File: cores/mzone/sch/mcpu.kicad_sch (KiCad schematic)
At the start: 45 parts

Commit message: mzone core
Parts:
- renumbered A_A13 to B_A13, A_A14 to B_A14, A_B12 to B_B12, A_B13 to B_B13, A_B7 to B_B7, A_C1 to B_C1, A_C10 to B_C10, A_C11 to B_C11, A_C12 to B_C12, A_C13 to B_C13, A_C9 to B_C9, A_D10 to B_D10, A_D14 to B_D14, A_D8 to B_D8, A_DE11 to B_DE11, A_DE12 to B_DE12, A_DE13 to B_DE13, A_DE9 to B_DE9, A_F10 to B_F10, A_F6 to B_F6, A_F9 to B_F9, A_FG14 to B_FG14, A_G6 to B_G6, A_G7 to B_G7, A_G8 to B_G8, A_G9 to B_G9, A_H10 to B_H10, A_H11 to B_H11, A_H12 to B_H12, A_H14 to B_H14, A_H6 to B_H6, A_H7 to B_H7, A_H8 to B_H8, A_RA7 to B_RA7

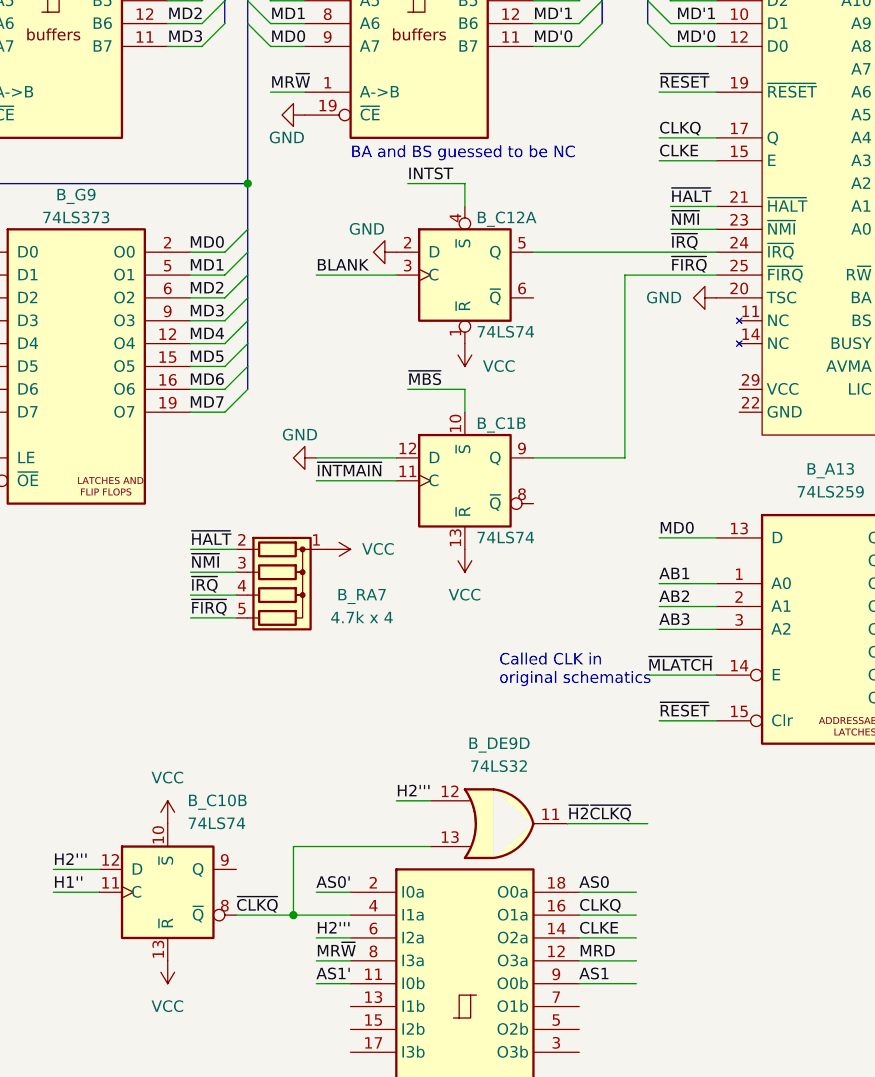
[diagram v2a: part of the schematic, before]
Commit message: mzone core
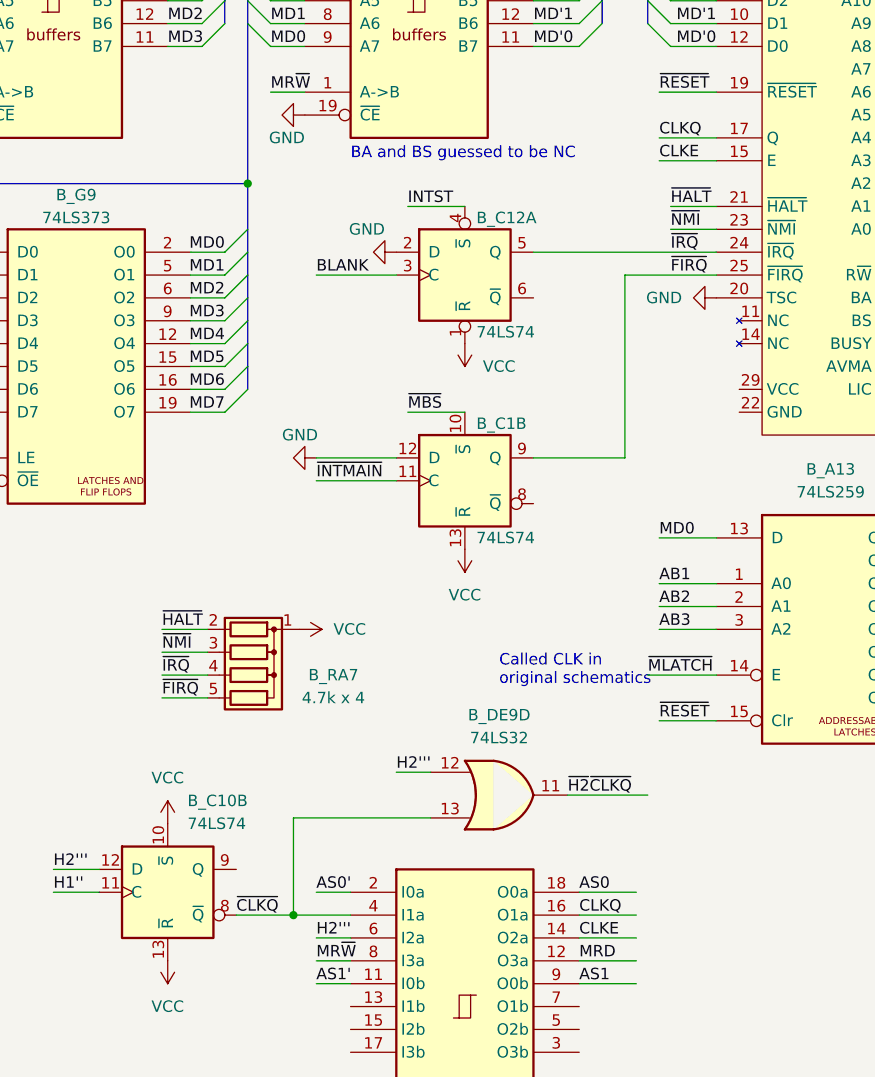
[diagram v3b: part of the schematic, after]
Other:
- moved on the sheet: B_DE9D, B_RA7
